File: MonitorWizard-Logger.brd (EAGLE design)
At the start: 125 x 80 mm, 41 parts, among them CON1 MICROSD, IC1 LD117AV33, J1 22-27-2041-04, J2 22-27-2041-04, J3 22-27-2041-04, U1 DHT22, U2 RFM69HW, U3 LTC3531, U4-NRF24L01 NRF24L01+-PCB-AERIAL, U6 ATMEGA328P-PU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

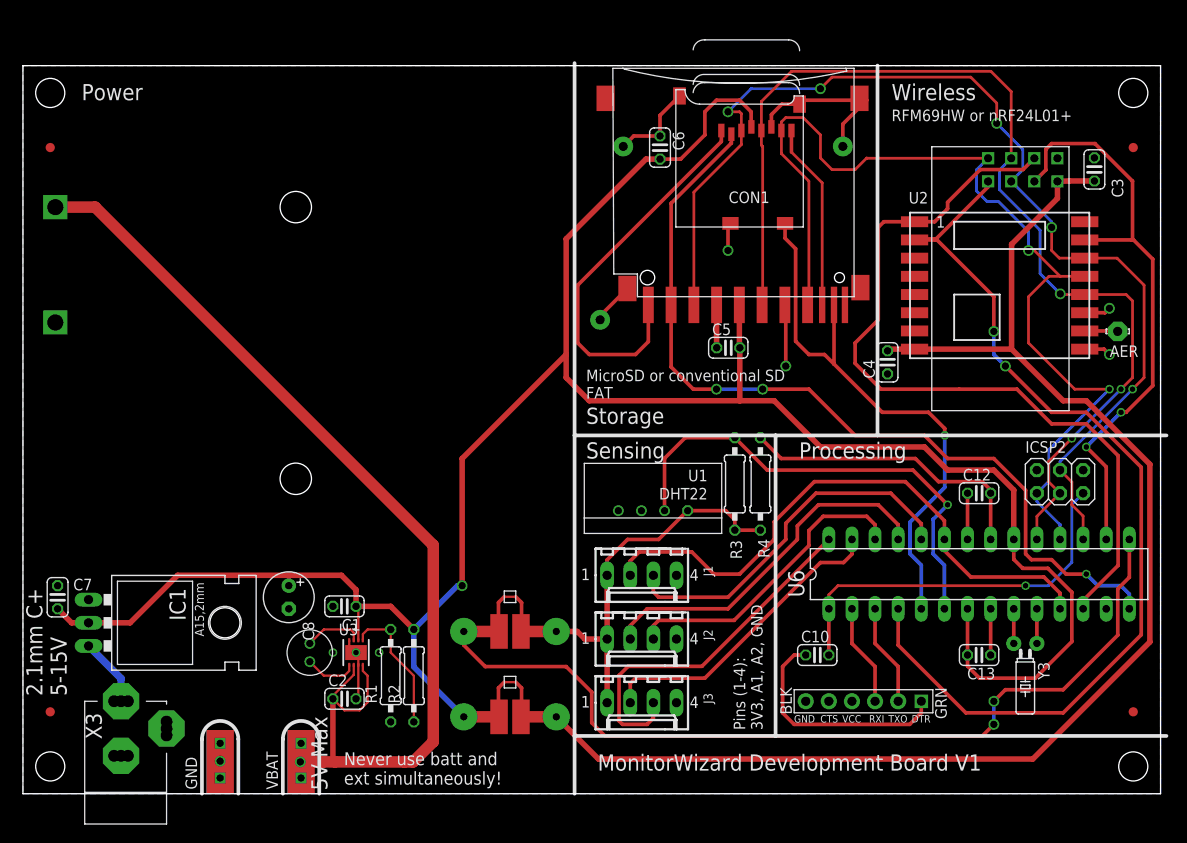
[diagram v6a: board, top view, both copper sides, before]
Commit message: Make the board smaller by pushing battery box to rear
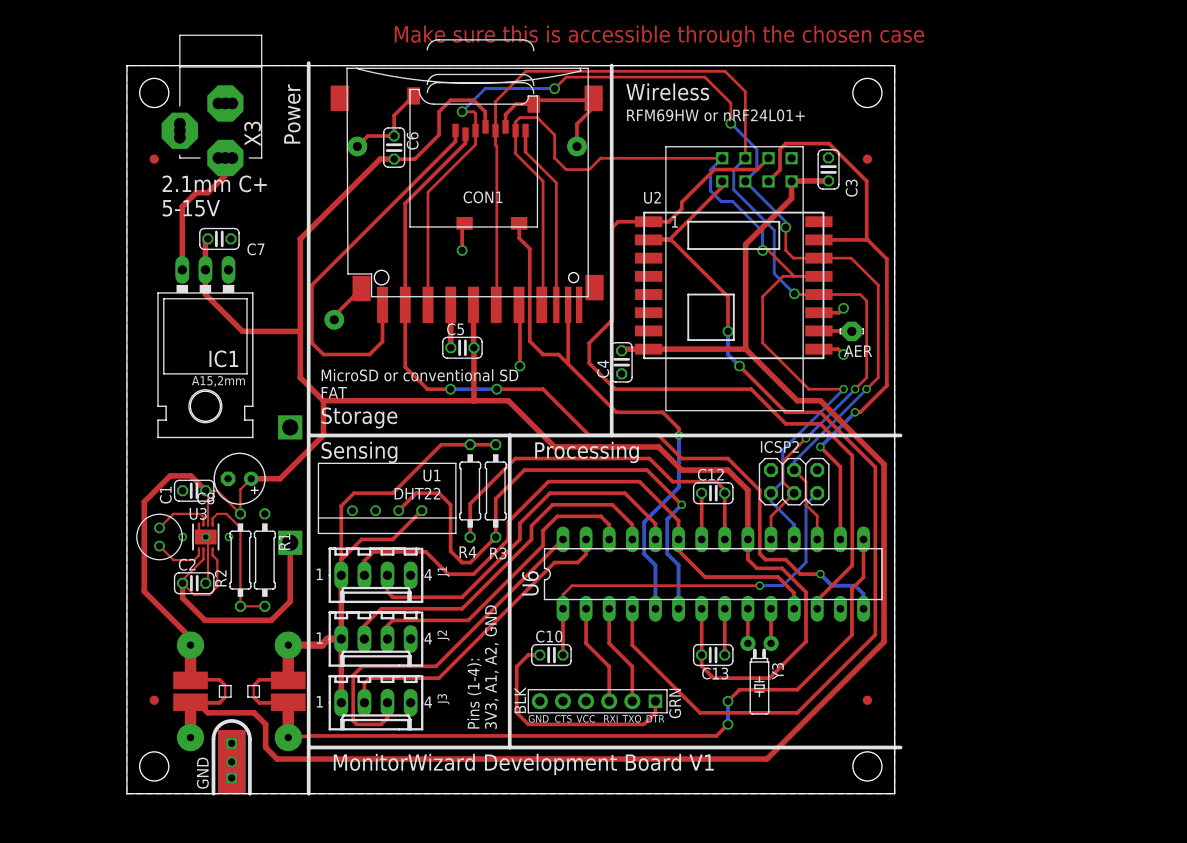
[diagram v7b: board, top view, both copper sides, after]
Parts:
- removed VBAT: ALLIGATOR, Probes:ALLIGATOR
- U$2: device keystone:2464 -> keystone-nodrills:2464
- U3: device linear-sen:DFN8-3X3 -> exported-lbrlinear-sen:DFN8-3X3
- moved X3 73.3 mm to (22.3, 76.2), turned to 0 degrees
- moved C7 43.2 mm to (21.6, 61.0), turned to 180 degrees
- moved IC1 36.1 mm to (20.1, 53.8), turned to 180 degrees
- moved I_RF 35.2 mm to (18.4, 11.2), turned to 0 degrees
- moved R4 31.9 mm to (49.1, 33.3), turned to 270 degrees
- moved FD1 29.2 mm to (92.8, 69.7)
- moved FD4 29.2 mm to (92.8, 10.3)
- moved AER 29.2 mm to (91.1, 50.8)
- moved C12 29.2 mm to (75.8, 33.0)
- moved C13 29.2 mm to (75.8, 15.2)
- moved C3 29.2 mm to (88.5, 68.6)
- moved ICSP2 29.2 mm to (84.7, 34.3)
- moved U$1 29.2 mm to (48.9, 54.6)
- moved U6 29.2 mm to (75.8, 24.1)
- moved C10 29.2 mm to (58.1, 15.2)
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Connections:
- net VBAT: no longer VBAT.BTM, VBAT.TOP
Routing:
- net VBAT: track 115.0 -> 35.6 mm, vias 1 -> 0
- net 3V3: track 251.2 -> 222.7 mm, vias 1 -> 0
- net SENSOR_3V3: track 42.3 -> 60.3 mm
- net SENSOR_POWER: track 97.0 -> 79.1 mm
- net RFMODULE_3V3: track 150.7 -> 167.5 mm
- net AREF: track 33.1 -> 40.6 mm
- net VBJ: track 7.56 -> 15.0 mm
- net DHT22_DATA: track 53.4 -> 58.9 mm
- net GND: track 71.8 -> 74.3 mm
- net N$3: track 15.2 -> 15.9 mm
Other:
- board size 125 x 80 mm -> 84.4 x 80 mm
- board text added: "Make sure this is accessible through the chosen case"
- board text removed: "5V Max"
- board text removed: "Never use batt and ext simultaneously!"
- board text removed: "Not heatsinked - current draw should not be significant enough to warrant heatsinking, even at higher voltage inputs."

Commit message: Shrink board, move barrel jack out of way of screw head
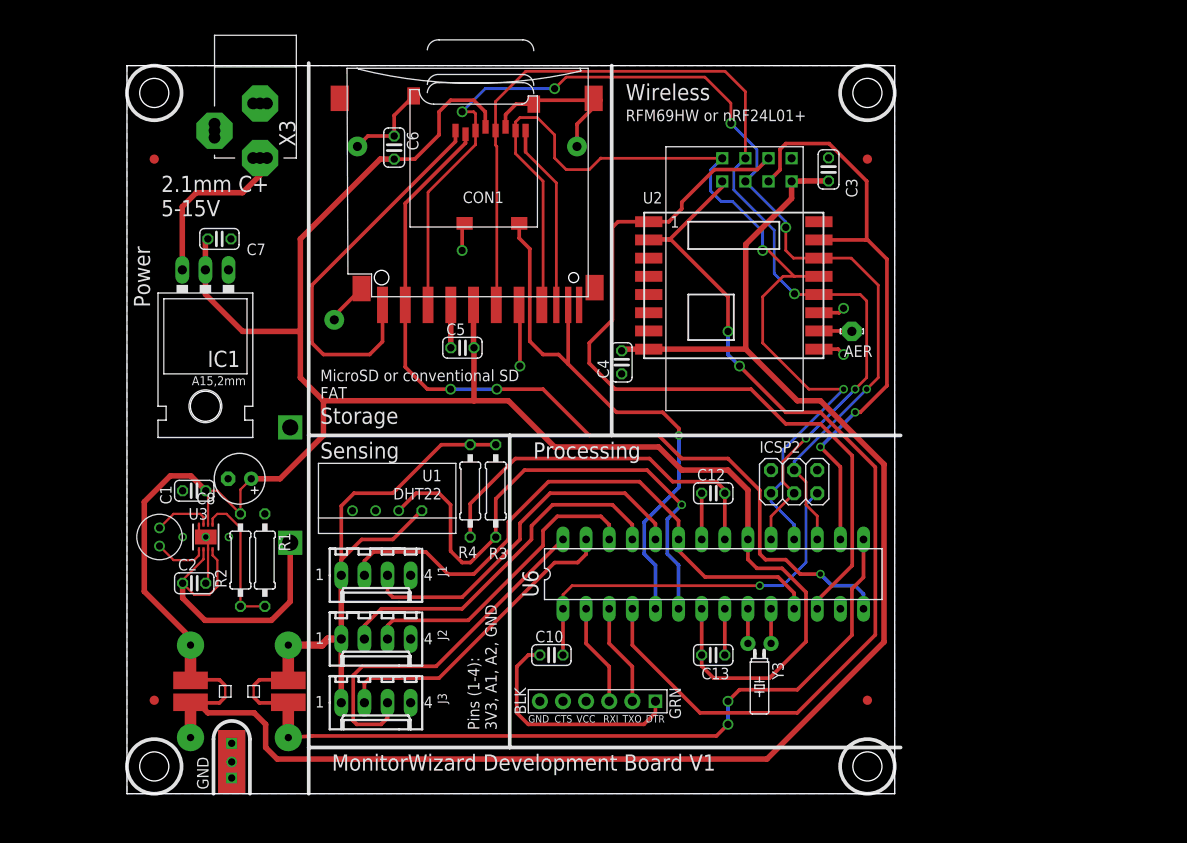
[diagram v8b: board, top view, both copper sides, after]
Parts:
- moved X3 3.81 mm to (26.1, 76.2)
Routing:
- net VBJ: track 15.0 -> 18.8 mm
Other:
- board text removed: "Make sure this is accessible through the chosen case"
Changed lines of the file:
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@@
 5-15V</text>
 <text x="66.23" y="76.2" size="1.778" layer="21" font="vector">Wireless</text>
-<text x="30.48" y="71.22" size="1.778" layer="21" font="vector" rot="R90">Power</text>
+<text x="13.97" y="53.44" size="1.778" layer="21" font="vector" rot="R90">Power</text>
 <wire x1="31.4" y1="5.08" x2="31.4" y2="39.37" width="0.4064" layer="21"/>
 <wire x1="31.4" y1="39.37" x2="31.4" y2="80.28" width="0.4064" layer="21"/>
@@
 3V3, A1, A2, GND</text>
 <text x="66.23" y="73.9" size="1.27" layer="25" font="vector">RFM69HW or nRF24L01+</text>
-<text x="40.64" y="82.55" size="1.778" layer="1">Make sure this is accessible through the chosen case</text>
+<circle x="14.43" y="3" radius="3" width="0.4064" layer="21"/>
+<circle x="14.43" y="77" radius="3" width="0.4064" layer="21"/>
+<circle x="92.79" y="77" radius="3" width="0.4064" layer="21"/>
+<circle x="92.79" y="3" radius="3" width="0.4064" layer="21"/>
 </plain>
 <attributes>
@@
 </element>
 <element name="GND" library="Probes" package="ALLIGATOR" value="ALLIGATOR" x="22.94" y="0"/>
-<element name="X3" library="SmartPrj" package="POWERSUPPLY_DC-21MM" value="POWERSUPPLY_DC21MMX" x="22.32" y="76.2" smashed="yes">
-<attribute name="NAME" x="26.13" y="71.12" size="1.778" layer="25" ratio="5" rot="R90"/>
+<element name="X3" library="SmartPrj" package="POWERSUPPLY_DC-21MM" value="POWERSUPPLY_DC21MMX" x="26.13" y="76.2" smashed="yes">
+<attribute name="NAME" x="29.94" y="71.12" size="1.778" layer="25" ratio="5" rot="R90"/>
 </element>
 <element name="FD4" library="SmartPrj" package="FIDUCIA-MOUNT" value="FIDUCIALMOUNT" x="92.79" y="10.27"/>
@@
 <wire x1="17.51" y1="57.56" x2="17.51" y2="64.5" width="0.6096" layer="1"/>
 <wire x1="17.51" y1="64.5" x2="19.05" y2="66.04" width="0.6096" layer="1"/>
-<wire x1="19.05" y1="66.04" x2="20.32" y2="66.04" width="0.6096" layer="1"/>
-<wire x1="20.32" y1="66.04" x2="22.2438" y2="67.9638" width="0.6096" layer="1"/>
-<wire x1="22.2438" y1="67.9638" x2="22.2438" y2="69.85" width="0.6096" layer="1"/>
+<wire x1="19.05" y1="66.04" x2="24.13" y2="66.04" width="0.6096" layer="1"/>
+<wire x1="24.13" y1="66.04" x2="26.0538" y2="67.9638" width="0.6096" layer="1"/>
+<wire x1="26.0538" y1="67.9638" x2="26.0538" y2="69.85" width="0.6096" layer="1"/>
 </signal>
 <signal name="DHT22_DATA">
